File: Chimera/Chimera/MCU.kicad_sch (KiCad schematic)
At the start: 41 parts, among them J10 DM3CS-SF, J11 Reciver, J12 Micro_SD_Card, J8 Button, J9 USB_B_Micro, U3 RP2040, U8 W25Q128JVSIQ, U9 OpAmp, X1 ABM8-272-T3

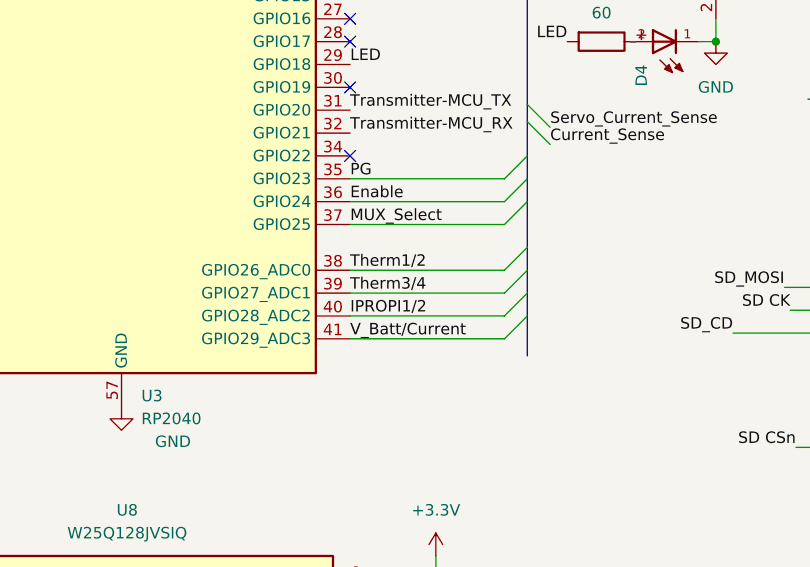
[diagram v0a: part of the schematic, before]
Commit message: Finalized MUX and thermistor wiring, Need to revise Buck and add Opamp surronding circuitry
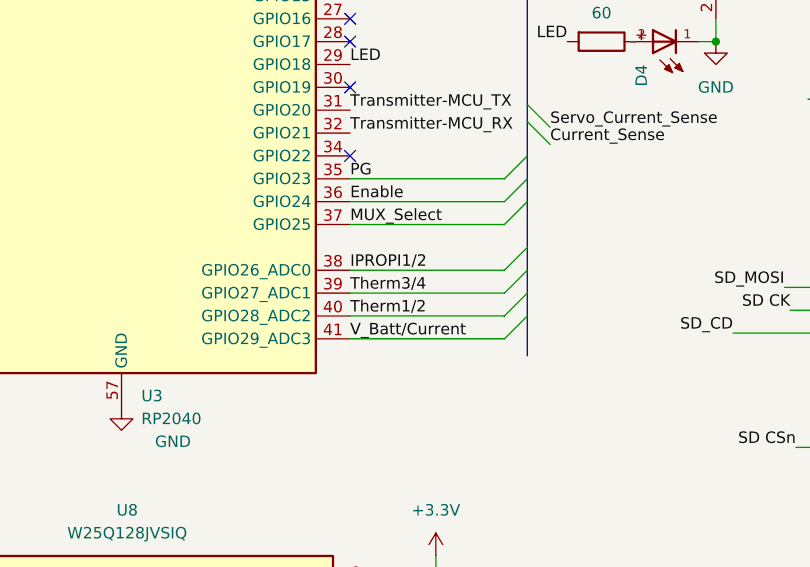
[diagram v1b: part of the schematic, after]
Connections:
- net IPROPI1/2: now also U3.38 (GPIO26_ADC0); no longer U3.40 (GPIO28_ADC2)
- net Therm1/2: now also U3.40 (GPIO28_ADC2); no longer U3.38 (GPIO26_ADC0)
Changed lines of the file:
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@@
+    (effects (font (size 1.27 1.27)) (justify left bottom))
+  )
+  (label "Therm1{slash}2" (at 121.92 123.19 0) (fields_autoplaced)
     (effects (font (size 1.27 1.27)) (justify left bottom))
   )
@@
     (effects (font (size 1.27 1.27)) (justify left bottom))
   )
-  (label "Therm3{slash}4" (at 121.92 120.65 0) (fields_autoplaced)
-    (effects (font (size 1.27 1.27)) (justify left bottom))
-  )
   (label "SD CSn" (at 171.45 137.795 180) (fields_autoplaced)
     (effects (font (size 1.27 1.27)) (justify right bottom))
@@
   )
   (label "SD_MOSI" (at 121.92 87.63 0) (fields_autoplaced)
-    (effects (font (size 1.27 1.27)) (justify left bottom))
-  )
-  (label "Therm1{slash}2" (at 121.92 118.11 0) (fields_autoplaced)
     (effects (font (size 1.27 1.27)) (justify left bottom))
   )
@@
     (effects (font (size 1.27 1.27)) (justify right bottom))
   )
-  (label "IPROPI1{slash}2" (at 121.92 123.19 0) (fields_autoplaced)
-    (effects (font (size 1.27 1.27)) (justify left bottom))
-  )
   (label "Enable" (at 121.92 110.49 0) (fields_autoplaced)
     (effects (font (size 1.27 1.27)) (justify left bottom))
@@
     (effects (font (size 1.27 1.27)) (justify left bottom))
   )
+  (label "V_Batt{slash}Current" (at 121.92 125.73 0) (fields_autoplaced)
+    (effects (font (size 1.27 1.27)) (justify left bottom))
+  )
   (label "SD_CD" (at 164.465 125.095 180) (fields_autoplaced)
     (effects (font (size 1.27 1.27)) (justify right bottom))
   )
   (label "Transmitter-MCU_TX" (at 121.92 100.33 0) (fields_autoplaced)
+    (effects (font (size 1.27 1.27)) (justify left bottom))
+  )
+  (label "Therm3{slash}4" (at 121.92 120.65 0) (fields_autoplaced)
     (effects (font (size 1.27 1.27)) (justify left bottom))
   )
@@
     (effects (font (size 1.27 1.27)) (justify left bottom))
   )
+  (label "IPROPI1{slash}2" (at 121.92 118.11 0) (fields_autoplaced)
+    (effects (font (size 1.27 1.27)) (justify left bottom))
+  )
   (label "LED" (at 121.92 95.25 0) (fields_autoplaced)
     (effects (font (size 1.27 1.27)) (justify left bottom))
@@
     (effects (font (size 1.27 1.27)) (justify right bottom))
   )
-  (label "V_Batt{slash}Current" (at 121.92 125.73 0) (fields_autoplaced)
-    (effects (font (size 1.27 1.27)) (justify left bottom))
-  )
   (label "QSPI_SD1" (at 71.12 74.93 180) (fields_autoplaced)

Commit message: Final Board and BOM
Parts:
- removed J12: Micro_SD_Card, symbol Connector:Micro_SD_Card
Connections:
- net at J9.3 (D+), R32.1: now also D5.2 (A2)
- net at D6.2 (A2), J9.2 (D-), R33.2: no longer D5.2 (A2)
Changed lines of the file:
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@@
   (junction (at 153.67 31.115) (diameter 0) (color 0 0 0 0)
   )
+  (junction (at 55.245 57.15) (diameter 0) (color 0 0 0 0)
+  )
   (junction (at 81.915 18.415) (diameter 0) (color 0 0 0 0)
   )
@@
   )
   (junction (at 163.195 31.115) (diameter 0) (color 0 0 0 0)
-  )
-  (junction (at 55.245 59.69) (diameter 0) (color 0 0 0 0)
   )
   (junction (at 133.985 31.115) (diameter 0) (color 0 0 0 0)
@@
     (stroke (width 0) (type default))
   )
-  (wire (pts (xy 55.245 59.69) (xy 56.515 59.69))
+  (wire (pts (xy 51.435 59.69) (xy 56.515 59.69))
     (stroke (width 0) (type default))
   )
@@
     (stroke (width 0) (type default))
   )
+  (wire (pts (xy 55.245 57.15) (xy 56.515 57.15))
+    (stroke (width 0) (type default))
+  )
   (wire (pts (xy 52.07 157.48) (xy 57.785 157.48))
     (stroke (width 0) (type default))
@@
     (stroke (width 0) (type default))
   )
+  (wire (pts (xy 55.245 57.15) (xy 55.245 62.865))
+    (stroke (width 0) (type default))
+  )
   (wire (pts (xy 71.12 104.14) (xy 71.12 105.41))
     (stroke (width 0) (type default))
@@
     (stroke (width 0) (type default))
   )
-  (wire (pts (xy 50.165 57.15) (xy 56.515 57.15))
+  (wire (pts (xy 50.165 57.15) (xy 55.245 57.15))
     (stroke (width 0) (type default))
   )
@@
     (stroke (width 0) (type default))
   )
-  (wire (pts (xy 55.245 59.69) (xy 55.245 62.865))
-    (stroke (width 0) (type default))
-  )
   (bus (pts (xy 141.605 62.23) (xy 141.605 64.77))
     (stroke (width 0) (type default))
@@
   )
   (bus (pts (xy 141.605 72.39) (xy 141.605 99.695))
-    (stroke (width 0) (type default))
-  )
-  (wire (pts (xy 51.435 59.69) (xy 55.245 59.69))
     (stroke (width 0) (type default))
   )
@@
         )
       )
-    )
-  )
-  (symbol (lib_id "Connector:Micro_SD_Card") (at 244.475 135.89 0) (unit 1)
-    (in_bom yes) (on_board yes) (dnp no) (fields_autoplaced)
-    (property "Reference" "J12" (at 245.11 116.84 0)
-      (effects (font (size 1.27 1.27)))
-    )
-    (property "Value" "Micro_SD_Card" (at 245.11 119.38 0)
-      (effects (font (size 1.27 1.27)))
-    )
-    (property "Footprint" "" (at 273.685 128.27 0)
-      (effects (font (size 1.27 1.27)) hide)
-    )
-    (property "Datasheet" "http://katalog.we-online.de/em/datasheet/693072010801.pdf" (at 244.475 135.89 0)
-      (effects (font (size 1.27 1.27)) hide)
-    )
-    (pin "7")
-    (pin "5")
-    (pin "8")
-    (pin "6")
-    (pin "9")
-    (pin "4")
-    (pin "1")
-    (pin "2")
-    (pin "3")
-    (instances
-      (project "Chimera"
-        (path "/dfd9978a-0f69-4125-9852-5613922ebd2e/503ee186-53a5-4705-87a3-2a809af2778c"
-          (reference "J12") (unit 1)
-        )
-      )
